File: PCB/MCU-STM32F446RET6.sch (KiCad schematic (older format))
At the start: 48 parts, among them J3 20021121-00010C4LF, J4 0475890001-MicroUSBPort, P1 CONN_01X20, P2 CONN_01X20, SW1 B3U-1000P, U3 STM32F446RET6_-_TQFP64, X1 ABM3B8.000MHZB2T, X2 ABS07-32.768KHZ-9-T

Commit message: Board Size. Routing and Antenna
Board Size tweaked. More signals routed. Next will be pin swapping and
routing finished. Also experimented with importing a PCB antenna design
from bitmap, still can't get it quite right, hopefully nex commit.
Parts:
- removed P1, P2: CONN_01X20, Pin_Headers:Pin_Header_Straight_1x20, symbol CONN_01X20
- added P1, P2: CONN_01X18, symbol CONN_01X18
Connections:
- wire segments 183 -> 207
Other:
- moved on the sheet: FD1, FD2, FD3, H1, H2, H3, H4, SW1

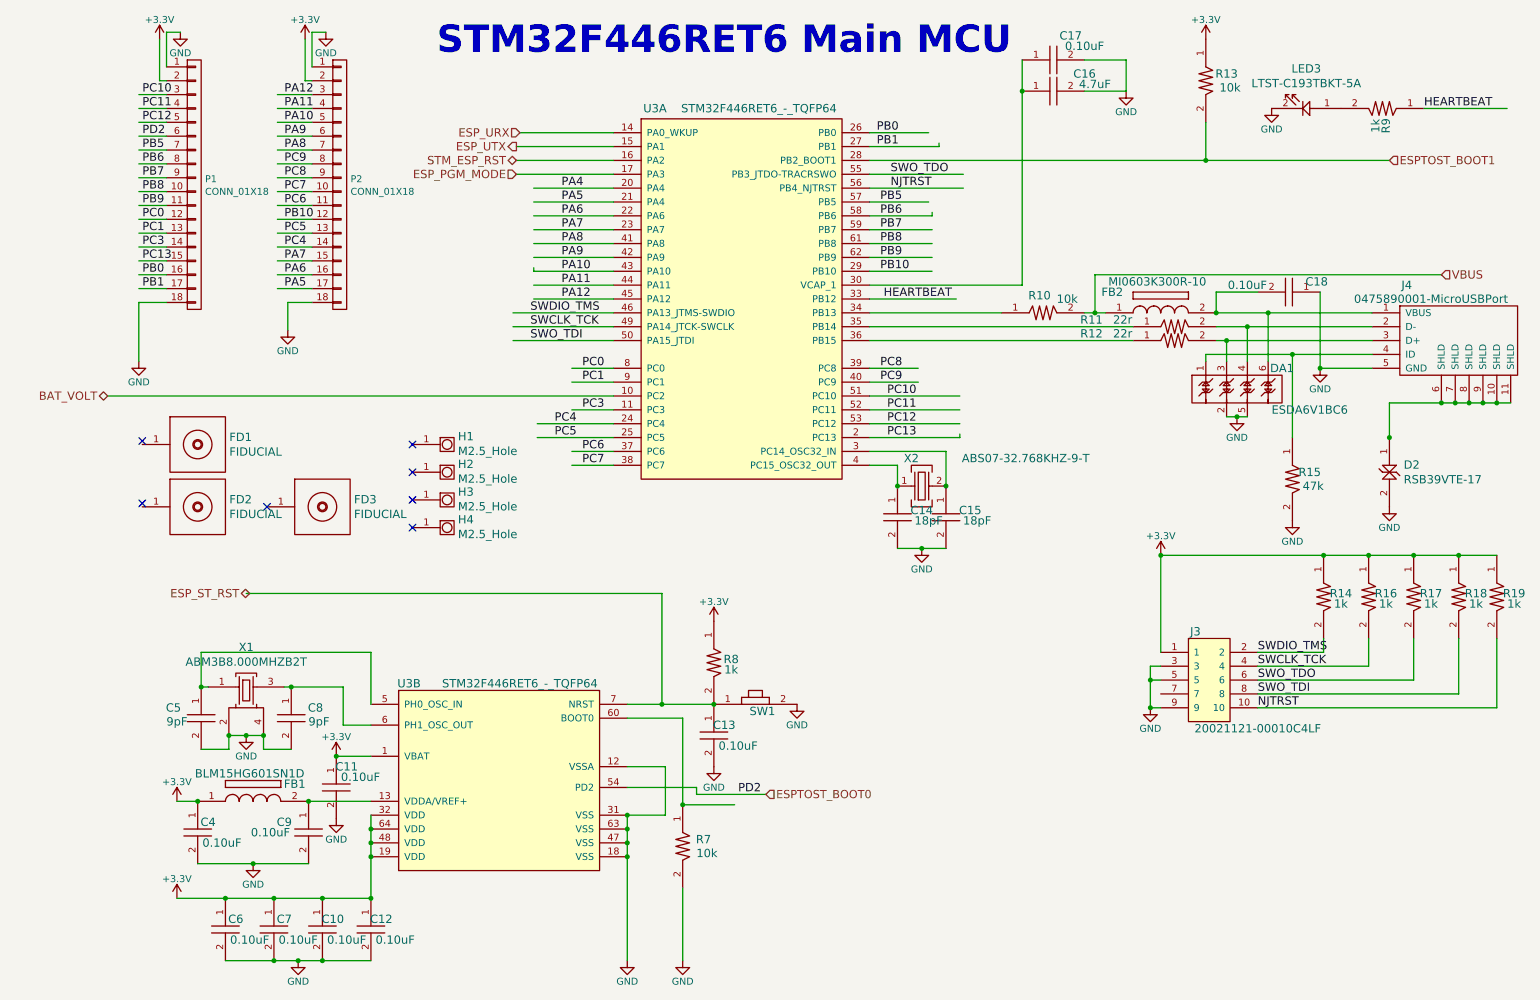
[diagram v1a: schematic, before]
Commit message: More routing
more routing completed, but thinking of scraping the current pass
entirely and rechoosing all the pins.
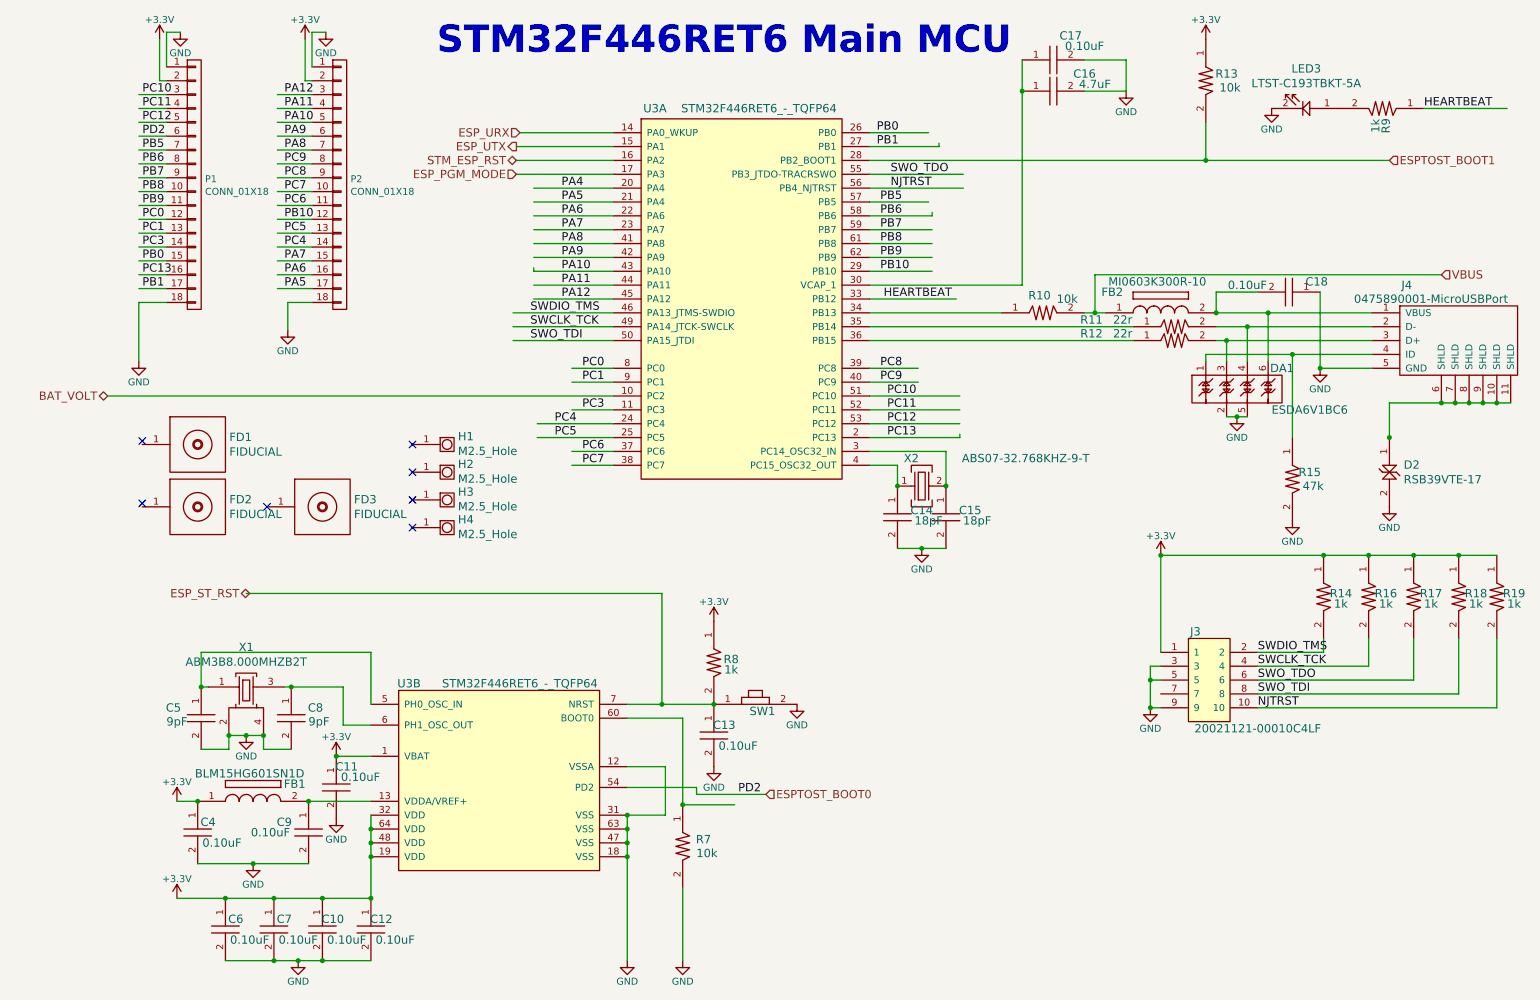
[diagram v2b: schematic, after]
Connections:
- wire segments 207 -> 172
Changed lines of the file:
@@
 	2875 6275 2425 6275
 Wire Wire Line
-	1625 6725 2025 6725
-Wire Wire Line
-	2025 6725 2425 6725
+	1625 6725 2425 6725
 Connection ~ 2025 6725
 Wire Wire Line
-	2875 6975 2875 6675
-Wire Wire Line
-	2875 6675 2875 6575
-Wire Wire Line
-	2875 6575 2875 6475
-Wire Wire Line
-	2875 6475 2875 6375
-Wire Wire Line
-	1475 6975 1825 6975
-Wire Wire Line
-	1825 6975 2175 6975
-Wire Wire Line
-	2175 6975 2525 6975
-Wire Wire Line
-	2525 6975 2875 6975
+	2875 6975 2875 6375
+Wire Wire Line
+	1475 6975 2875 6975
 Connection ~ 2875 6475
 Connection ~ 2875 6575
@@
 Connection ~ 2875 6975
 Wire Wire Line
-	1825 7425 2175 7425
-Wire Wire Line
-	2175 7425 2350 7425
-Wire Wire Line
-	2350 7425 2525 7425
-Wire Wire Line
-	2525 7425 2875 7425
+	1825 7425 2875 7425
 Connection ~ 2525 7425
 Connection ~ 2175 7425
@@
 Connection ~ 2425 6275
 Wire Wire Line
-	4725 5575 4975 5575
-Wire Wire Line
-	4975 5575 5350 5575
+	4725 5575 5350 5575
 Connection ~ 5350 5575
 Wire Wire Line
 	5950 5575 5950 5575
 Wire Wire Line
-	4725 6375 4725 6475
-Wire Wire Line
-	4725 6475 4725 6575
-Wire Wire Line
-	4725 6575 4725 6675
-Wire Wire Line
-	4725 6675 4725 7425
+	4725 6375 4725 7425
 Connection ~ 4725 6675
 Connection ~ 4725 6475
@@
 	1850 5900 1850 5800
 Wire Wire Line
-	1850 5800 1975 5800
-Wire Wire Line
-	1975 5800 2100 5800
+	1850 5800 2100 5800
 Wire Wire Line
 	2100 5800 2100 5900
@@
 Connection ~ 2100 5800
 Wire Wire Line
-	2250 5450 2300 5450
-Wire Wire Line
-	2300 5450 2675 5450
+	2250 5450 2675 5450
 Wire Wire Line
 	2675 5450 2675 5725
@@
 Connection ~ 6675 4000
 Wire Wire Line
-	6675 4450 6850 4450
-Wire Wire Line
-	6850 4450 7025 4450
+	6675 4450 7025 4450
 Connection ~ 6850 4450
 Wire Wire Line
@@
 Connection ~ 8100 2750
 Wire Wire Line
-	8025 2750 8100 2750
-Wire Wire Line
-	8100 2750 8175 2750
+	8025 2750 8175 2750
 Wire Wire Line
 	7425 2750 6475 2750
 Wire Wire Line
-	8975 2750 9350 2750
-Wire Wire Line
-	9350 2750 10100 2750
-Wire Wire Line
-	8975 2950 9050 2950
-Wire Wire Line
-	9050 2950 10100 2950
-Wire Wire Line
-	8900 3050 9525 3050
-Wire Wire Line
-	9525 3050 10100 3050
+	8975 2750 10100 2750
+Wire Wire Line
+	8975 2950 10100 2950
+Wire Wire Line
+	8900 3050 10100 3050
 Wire Wire Line
 	9525 3050 9525 3650
 Wire Wire Line
-	10225 3400 10600 3400
-Wire Wire Line
-	10600 3400 10700 3400
-Wire Wire Line
-	10700 3400 10800 3400
-Wire Wire Line
-	10800 3400 10900 3400
-Wire Wire Line
-	10900 3400 11000 3400
-Wire Wire Line
-	11000 3400 11100 3400
+	10225 3400 11100 3400
 Wire Wire Line
 	10225 3400 10225 3650
@@
 Connection ~ 9525 3050
 Wire Wire Line
-	8975 2850 9200 2850
-Wire Wire Line
-	9200 2850 10100 2850
+	8975 2850 10100 2850
 Connection ~ 9200 2850
 Wire Wire Line
-	9050 3500 9125 3500
-Wire Wire Line
-	9125 3500 9200 3500
+	9050 3500 9200 3500
 Connection ~ 9125 3500
 Wire Wire Line
 	8575 5300 8500 5300
 Wire Wire Line
-	8500 5300 8500 5400
-Wire Wire Line
-	8500 5400 8500 5600
+	8500 5300 8500 5600
 Wire Wire Line
 	8500 5600 8575 5600
@@
 	9275 5600 11000 5600
 Wire Wire Line
-	8575 4500 9750 4500
-Wire Wire Line
-	9750 4500 10075 4500
-Wire Wire Line
-	10075 4500 10400 4500
-Wire Wire Line
-	10400 4500 10725 4500
-Wire Wire Line
-	10725 4500 11000 4500
+	8575 4500 11000 4500
 Wire Wire Line
 	8575 4500 8575 5200
@@
 	8325 925  8025 925
 Wire Wire Line
-	7575 925  7575 1150
-Wire Wire Line
-	7575 1150 7575 2550
+	7575 925  7575 2550
 Connection ~ 7575 1150
 Wire Wire Line
@@
 Connection ~ 8500 5600
 Wire Wire Line
-	6475 1650 8900 1650
-Wire Wire Line
-	8900 1650 10225 1650
+	6475 1650 10225 1650
 Wire Wire Line
 	4625 3350 975  3350
@@
 Text Label 6600 3650 0    60   ~ 0
 PC13
-Text Label 1225 2375 0    60   ~ 0
+Text Label 1225 2475 0    60   ~ 0
 PC13
 Text Label 6525 1450 0    60   ~ 0
@@
 Text Label 1225 2575 0    60   ~ 0
 PB1
-Text Label 1225 2475 0    60   ~ 0
+Text Label 1225 2375 0    60   ~ 0
 PB0
 Wire Wire Line

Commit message: Updates
Changed board size, heavily altered schematic and pinning to be more
efficient. Program mode for ESP8285 is switched to GPIO0 being pulled
high 10k and toggled by STM32. Board at 30mm By 70.5mm. Also switching
to chip antenna next commit, expect updates to libraries.
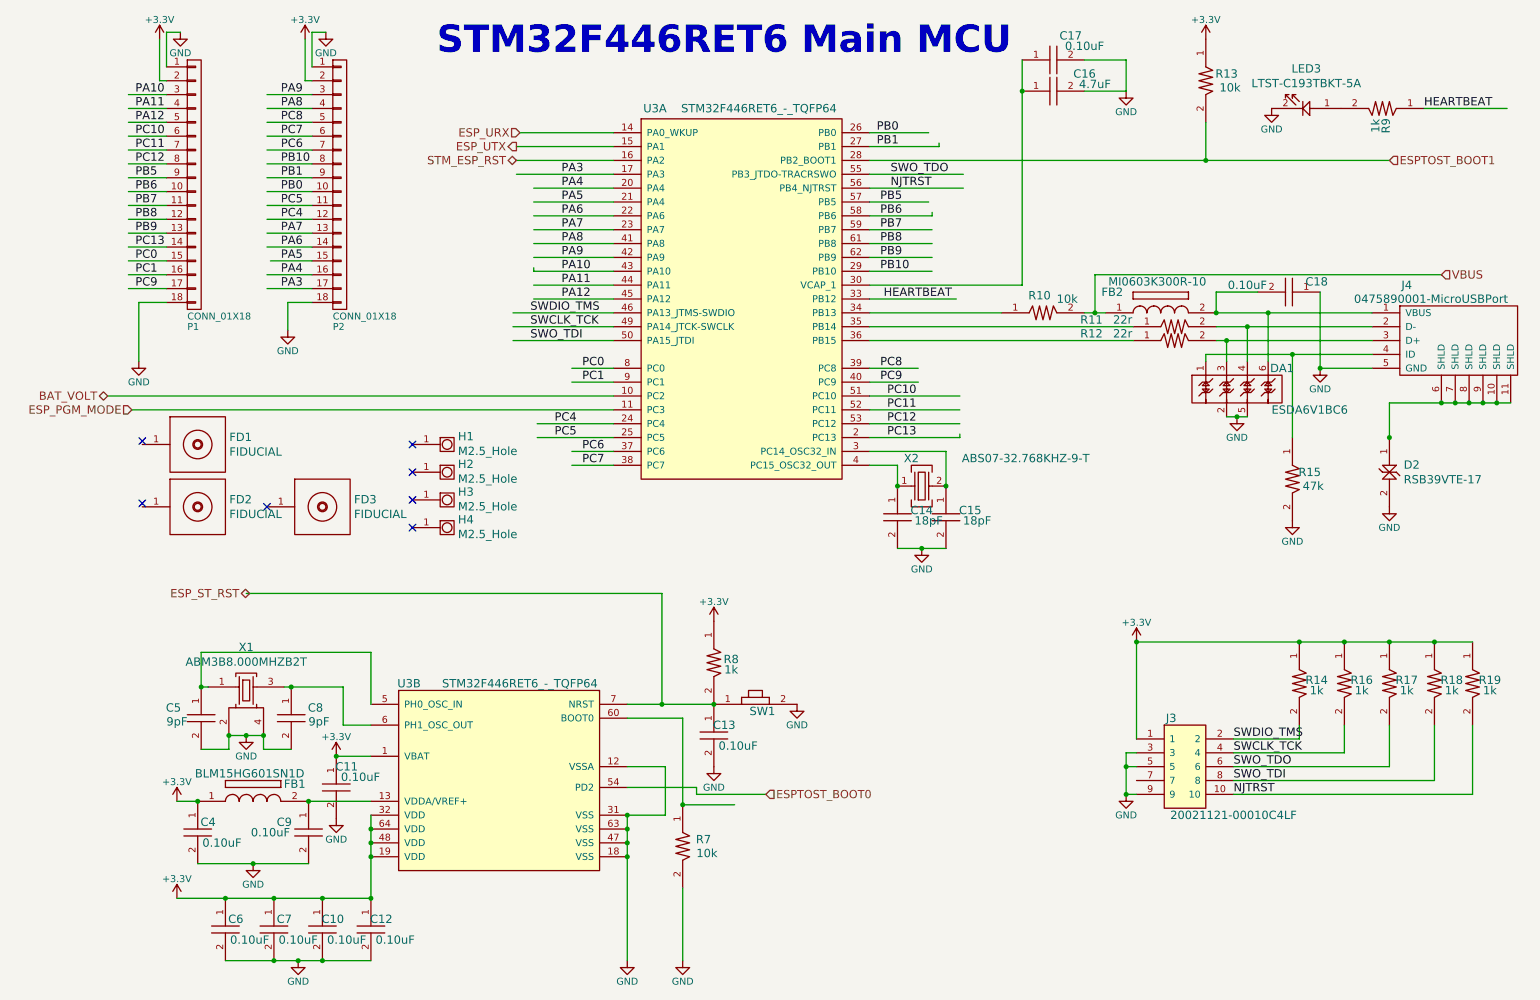
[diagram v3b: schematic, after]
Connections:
- net labels added: PA3
- net labels removed: PC3, PD2
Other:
- moved on the sheet: J3, R14, R16, R17, R18, R19
